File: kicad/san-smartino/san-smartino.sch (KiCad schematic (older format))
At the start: 47 parts, among them J1 GND CTS VBUS RX TX DTR, J2 SDA SCL -3V3 GND, J3 Conn_01x07_Male, SW1 Reset, SW2 Flash, U1 BQ27441DRZR-G1A, U2 ESP-12E, U3 LTC3440

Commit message: tiny updated
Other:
- note added: "Peripherals\n"
- note added: "Pin I/O"
- note removed: "Output\n\n"
- moved on the sheet: J2, J3
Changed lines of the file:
@@
 Wire Wire Line
 	7600 1500 7850 1500
-Text Notes 5250 4000 0    197  ~ 39
-Output\n\n
-Text Notes 5850 4050 0    118  ~ 24
+Text Notes 6700 3750 0    197  ~ 39
+Peripherals\n
+Text Notes 7450 4200 0    118  ~ 24
 I2C bus\n
 $Comp
 L Connector:Conn_01x04_Male J2
 U 1 1 604AEFED
-P 5650 4200
-F 0 "J2" H 5622 4082 50  0000 R CNN
-F 1 "SDA SCL -3V3 GND" H 5622 4173 50  0000 R CNN
-F 2 "Connector_PinHeader_2.54mm:PinHeader_1x04_P2.54mm_Vertical" H 5650 4200 50  0001 C CNN
-F 3 "~" H 5650 4200 50  0001 C CNN
-	1    5650 4200
+P 7250 4350
+F 0 "J2" H 7222 4232 50  0000 R CNN
+F 1 "SDA SCL -3V3 GND" H 7222 4323 50  0000 R CNN
+F 2 "Connector_PinHeader_2.54mm:PinHeader_1x04_P2.54mm_Vertical" H 7250 4350 50  0001 C CNN
+F 3 "~" H 7250 4350 50  0001 C CNN
+	1    7250 4350
 	-1   0    0    1
 $EndComp
-Text Label 5450 4000 2    79   ~ 0
+Text Label 7050 4150 2    79   ~ 0
 SDA
-Text Label 5450 4100 2    79   ~ 0
+Text Label 7050 4250 2    79   ~ 0
 SCL
 $Comp
 L power:+3.3V #PWR02
 U 1 1 604B144B
-P 5150 4200
-F 0 "#PWR02" H 5150 4050 50  0001 C CNN
-F 1 "+3.3V" H 5165 4373 50  0000 C CNN
-F 2 "" H 5150 4200 50  0001 C CNN
-F 3 "" H 5150 4200 50  0001 C CNN
-	1    5150 4200
+P 6750 4350
+F 0 "#PWR02" H 6750 4200 50  0001 C CNN
+F 1 "+3.3V" H 6765 4523 50  0000 C CNN
+F 2 "" H 6750 4350 50  0001 C CNN
+F 3 "" H 6750 4350 50  0001 C CNN
+	1    6750 4350
 	1    0    0    -1
 $EndComp
 Wire Wire Line
-	5150 4200 5450 4200
+	6750 4350 7050 4350
 $Comp
 L power:GND #PWR014
 U 1 1 604B5DAC
-P 5400 4300
-F 0 "#PWR014" H 5400 4050 50  0001 C CNN
-F 1 "GND" H 5405 4127 50  0000 C CNN
-F 2 "" H 5400 4300 50  0001 C CNN
-F 3 "" H 5400 4300 50  0001 C CNN
-	1    5400 4300
+P 7000 4450
+F 0 "#PWR014" H 7000 4200 50  0001 C CNN
+F 1 "GND" H 7005 4277 50  0000 C CNN
+F 2 "" H 7000 4450 50  0001 C CNN
+F 3 "" H 7000 4450 50  0001 C CNN
+	1    7000 4450
 	1    0    0    -1
 $EndComp
 Wire Wire Line
-	5400 4300 5450 4300
+	7000 4450 7050 4450
 $Comp
 L Connector:TestPoint TP4
@@
 	0    -1   -1   0
 $EndComp
-Text Label 5450 5050 2    79   ~ 0
+Text Label 7050 5200 2    79   ~ 0
 GPIO9
-Text Label 5450 5150 2    79   ~ 0
+Text Label 7050 5300 2    79   ~ 0
 GPIO10
-Text Label 5450 5350 2    79   ~ 0
+Text Label 7050 5500 2    79   ~ 0
 GPIO12
-Text Label 5450 5250 2    79   ~ 0
+Text Label 7050 5400 2    79   ~ 0
 GPIO13
-Text Label 5450 5450 2    79   ~ 0
+Text Label 7050 5600 2    79   ~ 0
 GPIO14
 $Comp
 L Connector:Conn_01x07_Male J3
 U 1 1 60537881
-P 5650 5150
-F 0 "J3" H 5622 5082 50  0000 R CNN
-F 1 "Conn_01x07_Male" H 5622 5173 50  0000 R CNN
-F 2 "Connector_PinHeader_2.54mm:PinHeader_1x07_P2.54mm_Vertical" H 5650 5150 50  0001 C CNN
-F 3 "~" H 5650 5150 50  0001 C CNN
-	1    5650 5150
+P 7250 5300
+F 0 "J3" H 7222 5232 50  0000 R CNN
+F 1 "Conn_01x07_Male" H 7222 5323 50  0000 R CNN
+F 2 "Connector_PinHeader_2.54mm:PinHeader_1x07_P2.54mm_Vertical" H 7250 5300 50  0001 C CNN
+F 3 "~" H 7250 5300 50  0001 C CNN
+	1    7250 5300
 	-1   0    0    1
 $EndComp
@@
 L power:+3.3V #PWR0108
 U 1 1 60539635
-P 5150 4950
-F 0 "#PWR0108" H 5150 4800 50  0001 C CNN
-F 1 "+3.3V" H 5165 5123 50  0000 C CNN
-F 2 "" H 5150 4950 50  0001 C CNN
-F 3 "" H 5150 4950 50  0001 C CNN
-	1    5150 4950
+P 6750 5100
+F 0 "#PWR0108" H 6750 4950 50  0001 C CNN
+F 1 "+3.3V" H 6765 5273 50  0000 C CNN
+F 2 "" H 6750 5100 50  0001 C CNN
+F 3 "" H 6750 5100 50  0001 C CNN
+	1    6750 5100
 	1    0    0    -1
 $EndComp
 Wire Wire Line
-	5150 4950 5450 4950
+	6750 5100 7050 5100
 Wire Notes Line
-	5000 1400 5000 9850
+	5150 -550 5150 7900
 $Comp
 L power:GND #PWR0109
 U 1 1 6053E170
-P 5450 4850
-F 0 "#PWR0109" H 5450 4600 50  0001 C CNN
-F 1 "GND" V 5455 4722 50  0000 R CNN
-F 2 "" H 5450 4850 50  0001 C CNN
-F 3 "" H 5450 4850 50  0001 C CNN
-	1    5450 4850
+P 7050 5000
+F 0 "#PWR0109" H 7050 4750 50  0001 C CNN
+F 1 "GND" V 7055 4872 50  0000 R CNN
+F 2 "" H 7050 5000 50  0001 C CNN
+F 3 "" H 7050 5000 50  0001 C CNN
+	1    7050 5000
 	0    1    1    0
 $EndComp
@@
 	1450 1200 1800 1200
 Connection ~ 1800 1200
+Text Notes 7400 5100 0    118  ~ 24
+Pin I/O
 $EndSCHEMATC

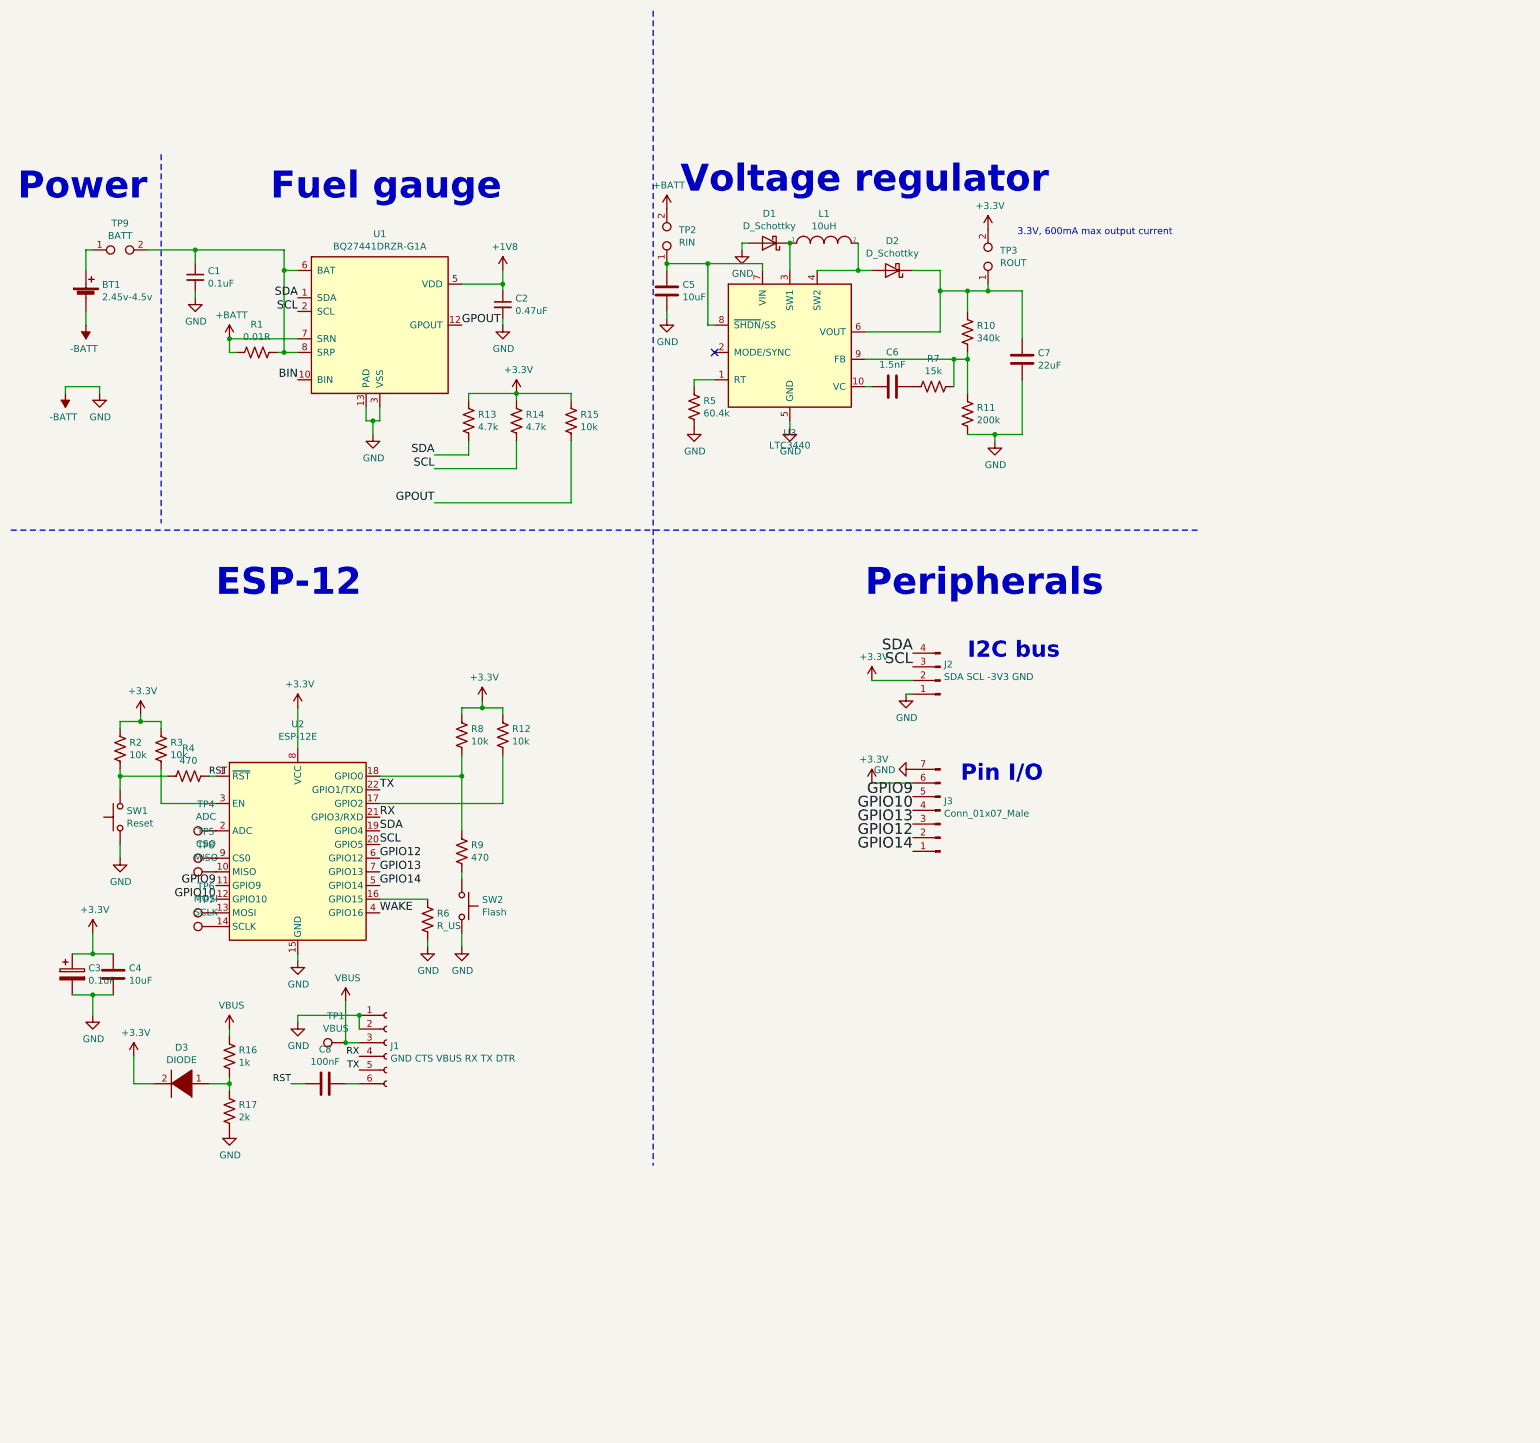
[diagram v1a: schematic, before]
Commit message: schematic updated, second battery and edgecut
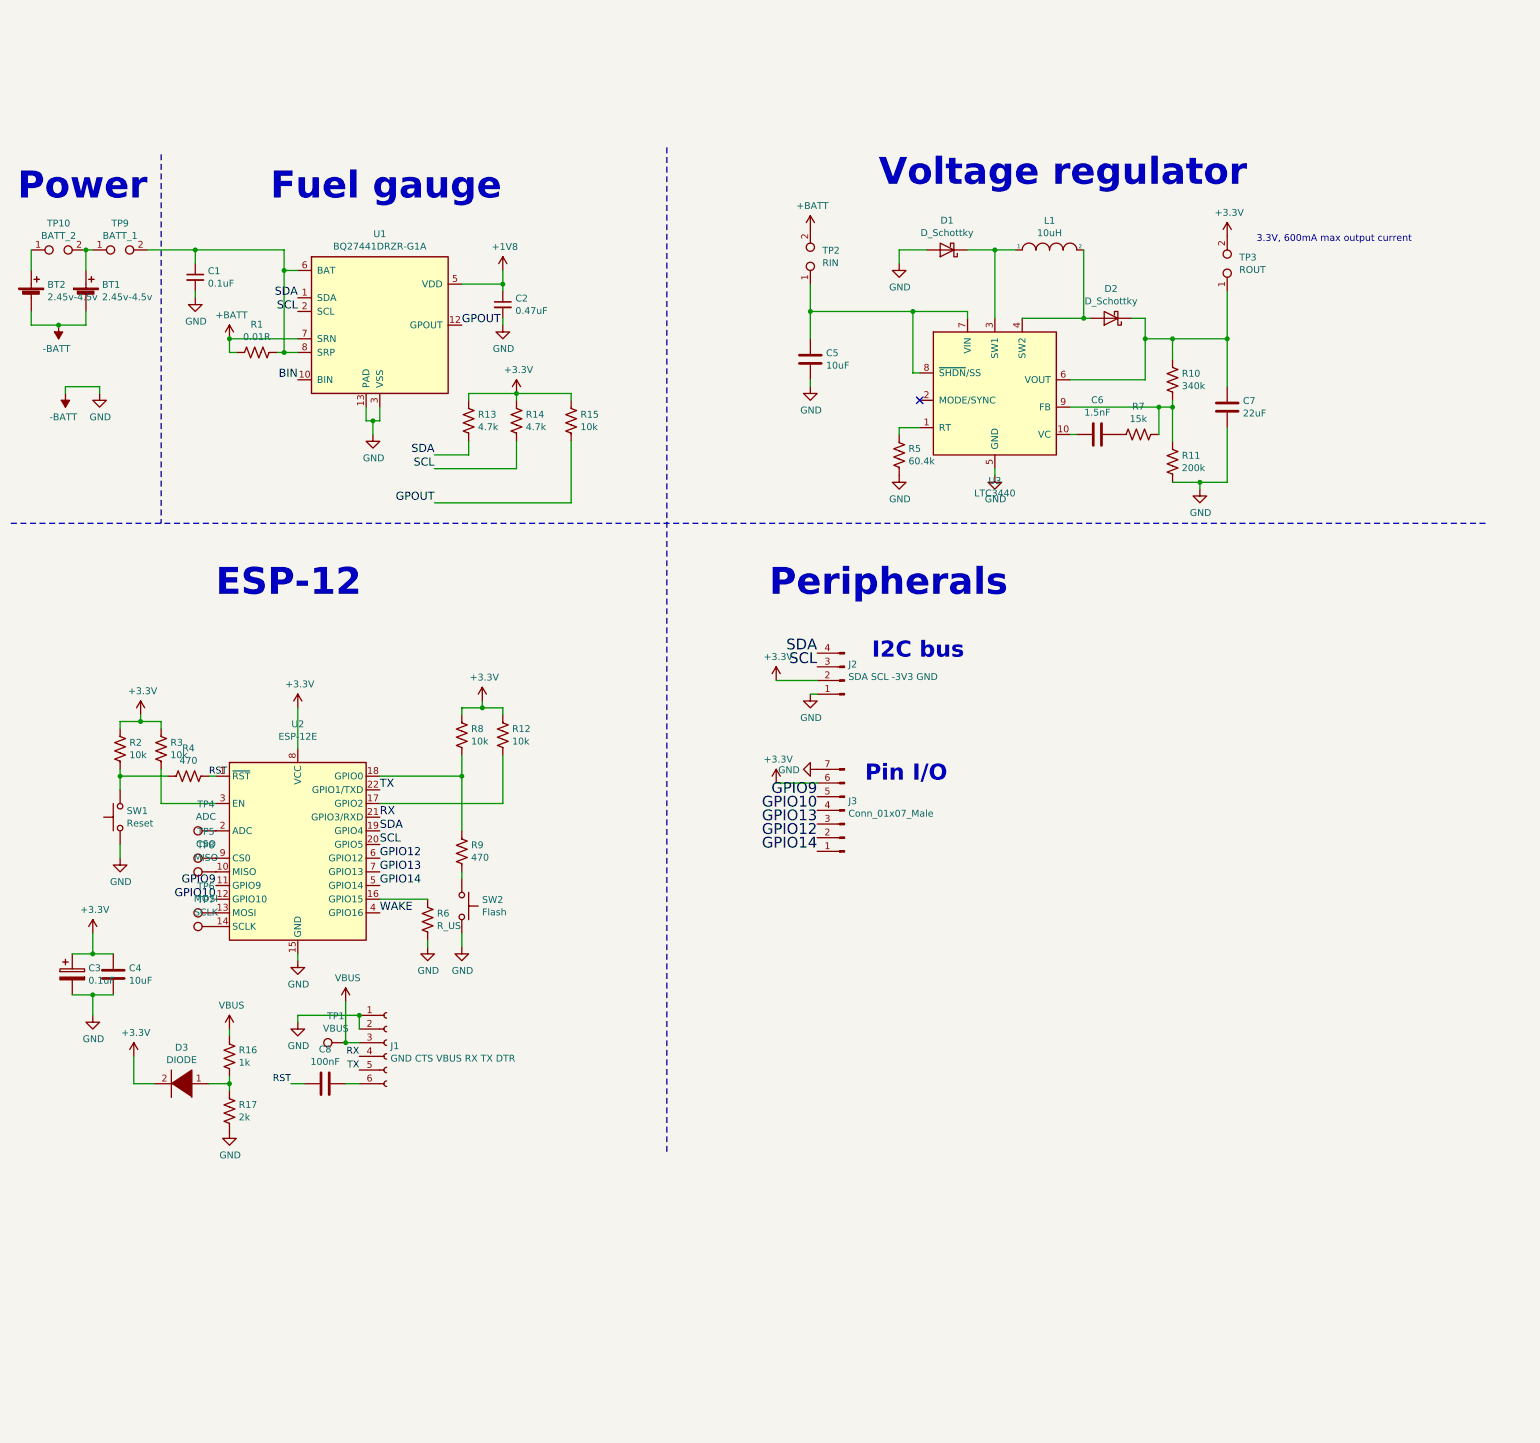
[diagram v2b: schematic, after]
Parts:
- added BT2: 2.45v-4.5v, san-smartino:18650-battery-metal-clips, symbol Device:Battery_Cell
- added TP10: BATT_2, TestPoint:TestPoint_2Pads_Pitch2.54mm_Drill0.8mm, symbol Connector:TestPoint_2Pole
- TP9: value BATT -> BATT_1
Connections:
- net -BATT: now also BT2.2 (-)
- net at BT1.1 (+), TP9.1: now also TP10.2
- new net: BT2.1 (+), TP10.1
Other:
- moved on the sheet: C5, C6, C7, D1, D2, J2, J3, L1, R10, R11, R5, R7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

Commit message: updated board
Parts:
- removed BT2: 2.45v-4.5v, san-smartino:18650-battery-metal-clips, symbol Device:Battery_Cell
- removed TP10: BATT_2, TestPoint:TestPoint_2Pads_Pitch2.54mm_Drill0.8mm, symbol Connector:TestPoint_2Pole
- added C10: 100nF, Capacitor_SMD:C_0805_2012Metric_Pad1.15x1.40mm_HandSolder, symbol Device:C
- added C11: 10uF, Capacitor_SMD:C_0805_2012Metric_Pad1.15x1.40mm_HandSolder, symbol Device:C
- added C9: 0.1uF, Capacitor_SMD:C_0805_2012Metric_Pad1.15x1.40mm_HandSolder, symbol Device:C
- added D4: STDBY, LED_SMD:LED_0603_1608Metric_Pad1.05x0.95mm_HandSolder, symbol Device:LED
- added D5: CHRG, LED_SMD:LED_0603_1608Metric_Pad1.05x0.95mm_HandSolder, symbol Device:LED
- added H1, H2, H3, H4: MountingHole, MountingHole:MountingHole_3.2mm_M3_Pad_Via, symbol Mechanical:MountingHole
- added J4: CHRG IN, Connector_PinHeader_2.54mm:PinHeader_1x02_P2.54mm_Vertical, symbol Connector:Conn_01x02_Female
- added J5: PW-SEL, Connector_PinHeader_2.54mm:PinHeader_1x03_P2.54mm_Vertical, symbol Connector:Conn_01x03_Male
- added R18: 1.2k, Resistor_SMD:R_0805_2012Metric_Pad1.15x1.40mm_HandSolder, symbol Device:R_US
- added R19, R20, R21: 1k, Resistor_SMD:R_0805_2012Metric_Pad1.15x1.40mm_HandSolder, symbol Device:R_US
- added R22: 100R, Resistor_SMD:R_0805_2012Metric_Pad1.15x1.40mm_HandSolder, symbol Device:R_US
- added TP10: Wake, TestPoint:TestPoint_Pad_D1.5mm, symbol Connector:TestPoint
- added U4: TP4056, Package_SO:SOP-8-1EP_4.57x4.57mm_P1.27mm_EP4.57x4.45mm, symbol tp4056:TP4056
- added U5: DW01, Package_TO_SOT_SMD:SOT-23-6_Handsoldering, symbol dw01:DW01
- added U6: FS8205A, Package_SO:TSSOP-8_4.4x3mm_P0.65mm, symbol fs8205a:FS8205A
- SW1: footprint Button_Switch_SMD:SW_SPST_CK_RS282G05A3 -> Button_Switch_SMD:SW_SPST_EVQP0
- TP9: value BATT_1 -> BATT
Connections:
- net WAKE: now also TP10.1
- net FUEL-GAUGE: now reaches C1.1, R1.1, U1.6 (BAT), U1.8 (SRP)
- net FUEL-GAUGE: now also J5.3 (Pin_3); no longer TP9.2
- net +BATT renamed VCC
- net VCC: now also J5.1 (Pin_1)
- net -BATT renamed GND
- net GND: now also C11.2, C9.2, J4.2 (Pin_2), R18.2, R21.2, U4.1 (TEMP), U4.3 (GND), U6.6 (S2), U6.7 (S2); no longer BT1.2 (-)
- net BIN: no longer names the net of U1.10 (BIN)
- new net: R18.1, U4.2 (PROG)
- new net: R19.2, U4.6 (~STDBY)
- new net: R20.2, U4.7 (~CHRG)
- new net: D4.1 (K), R19.1
- new net: D5.1 (K), R20.1
- new net: U5.1 (OD), U6.4 (G1)
- new net: R21.1, U5.2 (CS)
- new net: U5.3 (OC), U6.5 (G2)
- new net: C10.1, R22.2, U5.5 (VCC)
- new net BATT+: C11.1, J5.2 (Pin_2), R22.1, TP9.2, U4.5 (BAT)
- new net BATT-: BT1.2 (-), C10.2, U5.6 (GND), U6.2 (S1), U6.3 (S1)
- new net IN+: C9.1, D4.2 (A), D5.2 (A), J4.1 (Pin_1), U4.4 (VCC), U4.8 (CE), U4.9 (PP)
- no-connect marks 1 -> 5
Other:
- note added: "5v charger"
- note added: "Battery protection"
- moved on the sheet: BT1, C1, C2, C3, C4, C5, C6, C7, C8, D1, D2, D3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
